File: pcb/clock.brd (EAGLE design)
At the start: 0 parts

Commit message: Started PCB
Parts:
- added C1: 0.1uF, rcl:C025-025X050
- added C2, C3: 10uF, rcl:C025-025X050
- added C4: 1000uF, rcl:E3,5-8
- added CN1: (no value), adafruit:DCJACK_2MM_PTH
- added JP1: FTDI, pinhead:1X06/90
- added JP2: (no value), pinhead:1X02
- added JP3: 74AHCT125, ic-package:DIL14
- added R1, R3, R4, R5: 470, rcl:0207/10
- added R2: 10K, rcl:0207/10
- added U1: ESP-01, diy-modules:WIRELESS-WIFI-ESP-01
- added U2: LD1117V33, my-custom:TO-220
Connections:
- new net +5V: C1.1, C4.+, CN1.PWR, JP1.3, JP3.14, U2.P$3
- new net DTR: JP1.6
- new net GND: C1.2, C2.2, C3.2, C4.-, CN1.GND, JP1.1, JP1.2, JP2.2, JP3.1, JP3.4, JP3.7, R5.1, U1.A1, U2.P$1
- new net GNDBREAK: CN1.GNDBREAK
- new net GPIO2: JP3.2, U1.B1
- new net N$1: JP2.1, R1.2
- new net N$2: R2.1, U1.B2, U1.C2
- new net N$3: R4.1, R5.2
- new net NP_DATA: JP3.3, R1.1
- new net RXD_3V3: R3.1, R4.2, U1.D1
- new net RXD_5V: JP1.5, R3.2
- new net TXD_3V3: JP3.5, U1.A2
- new net TXD_5V: JP1.4, JP3.6
- new net VCC: C2.1, C3.1, R2.2, U1.D2, U2.P$2, U2.P$4
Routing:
- net VCC: track 0.00 -> 62.3 mm
- net GPIO2: track 0.00 -> 41.7 mm
- net TXD_5V: track 0.00 -> 30.3 mm
- net TXD_3V3: track 0.00 -> 26.9 mm
- net NP_DATA: track 0.00 -> 17.9 mm
- net RXD_3V3: track 0.00 -> 17.7 mm
- net N$2: track 0.00 -> 17.7 mm
- net RXD_5V: track 0.00 -> 8.89 mm
- net N$3: track 0.00 -> 4.45 mm
- net N$1: track 0.00 -> 3.81 mm
- added copper zone on layer 1, net +5V
- added copper zone on layer 16, net GND
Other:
- board outline added: 76.2 x 71.1 mm
- board text added: "5V"
- board text added: "BLK"
- board text added: "GND"
- board text added: "GRN"

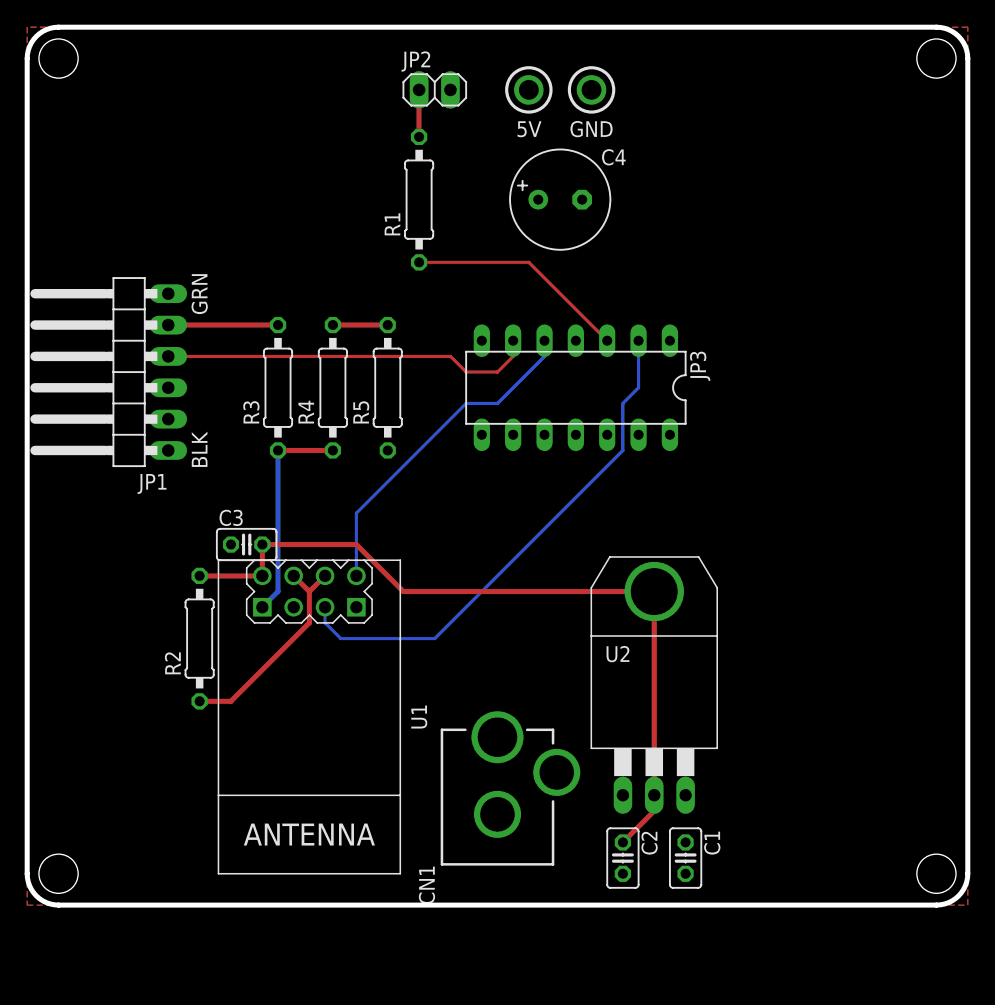
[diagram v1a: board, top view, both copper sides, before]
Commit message: Added button
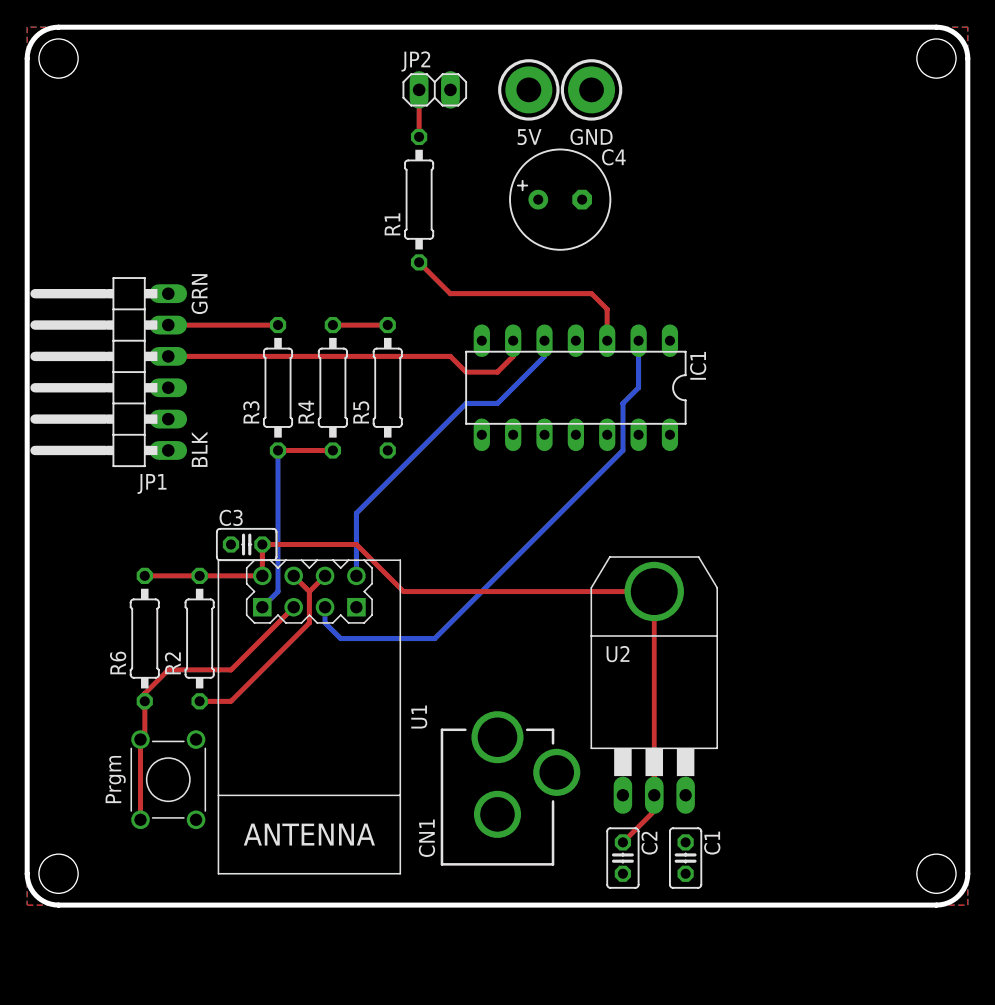
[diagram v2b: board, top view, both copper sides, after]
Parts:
- added R6: 10K, rcl:0207/10
- added S1: MJTP1230, my-custom:TACTILE-BUTTON-MJTP1230
- renumbered JP3 to IC1
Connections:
- new net GPIO0: R6.1, S1.P$1, S1.P$3, U1.C1
- net GND: now also S1.P$2, S1.P$4
- net VCC: now also R6.2
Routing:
- net GPIO0: track 0.00 -> 25.3 mm
- net VCC: track 62.3 -> 66.8 mm
- net NP_DATA: track 17.9 -> 19.4 mm
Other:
- board text added: "Prgm"

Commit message: Linearized the board layout
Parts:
- moved C4 44.5 mm to (41.9, 12.7)
- moved JP2 44.5 mm to (33.0, 21.6)
- moved JP1 42.0 mm to (10.2, 1.27), turned to 180 degrees
- moved R1 36.4 mm to (24.1, 21.6), turned to 180 degrees
- moved R6 36.1 mm to (41.9, 5.71), turned to 0 degrees
- moved IC1 33.8 mm to (25.4, 14.0)
- moved R2 33.8 mm to (41.9, 2.54), turned to 0 degrees
- moved C3 30.3 mm to (34.3, 3.81), turned to 90 degrees
- moved R5 28.8 mm to (7.62, 22.9), turned to 180 degrees
- moved R3 28.4 mm to (7.62, 16.5), turned to 180 degrees
- moved R4 28.1 mm to (7.62, 19.7), turned to 0 degrees
- moved CN1 25.4 mm to (63.5, 0.00)
- moved C2 20.1 mm to (59.7, 20.3), turned to 0 degrees
- moved C1 20.1 mm to (59.7, 22.9), turned to 180 degrees
- moved U2 5.68 mm to (53.3, 17.8), turned to 180 degrees
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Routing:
- net GPIO2: track 41.7 -> 16.1 mm
- net NP_DATA: track 19.4 -> 4.34 mm
- net TXD_5V: track 30.3 -> 18.9 mm
- net RXD_3V3: track 17.7 -> 28.1 mm
- net RXD_5V: track 8.89 -> 19.1 mm
- net N$1: track 3.81 -> 13.8 mm
- net VCC: track 66.8 -> 57.7 mm
- net TXD_3V3: track 26.9 -> 18.6 mm
- net GPIO0: track 25.3 -> 32.9 mm
- net N$2: track 17.7 -> 13.8 mm
- net N$3: track 4.45 -> 3.18 mm
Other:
- board size 76.2 x 71.1 mm -> 76.2 x 25.4 mm

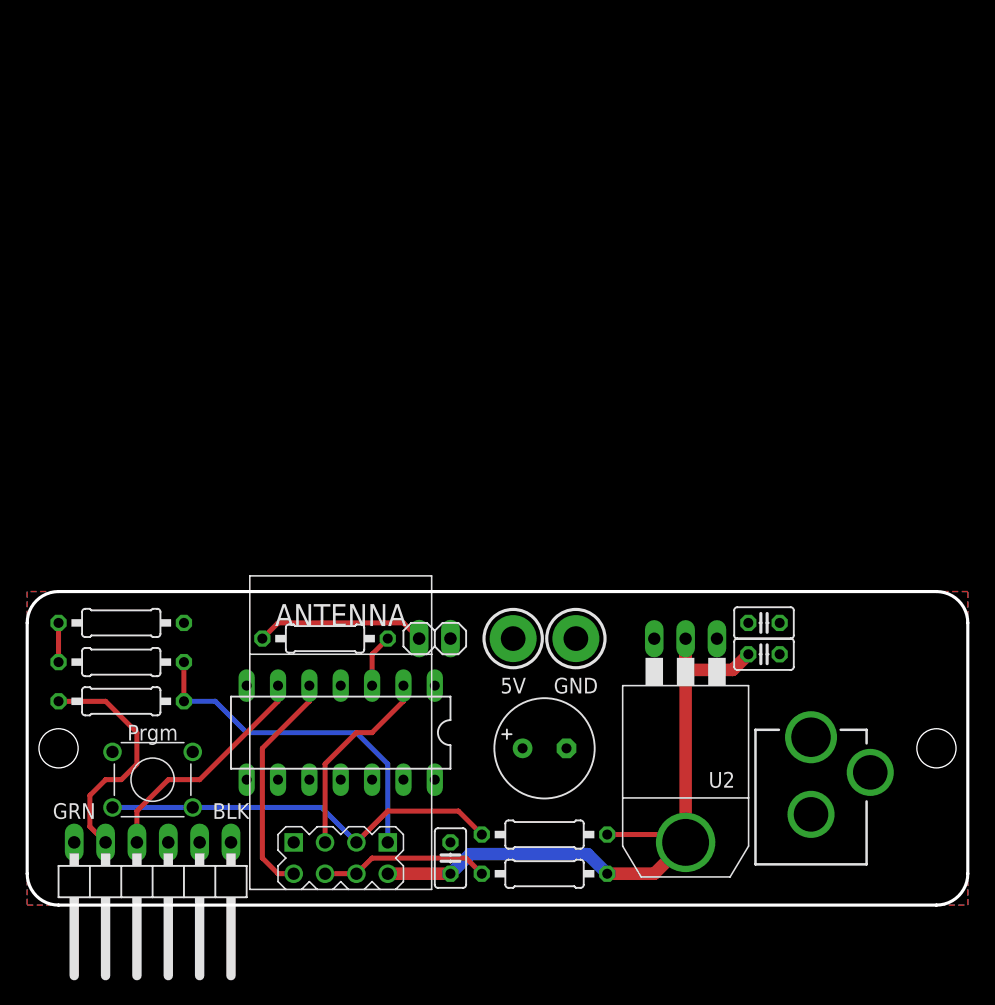
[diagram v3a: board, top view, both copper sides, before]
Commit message: Improved layout to make room for light sensor
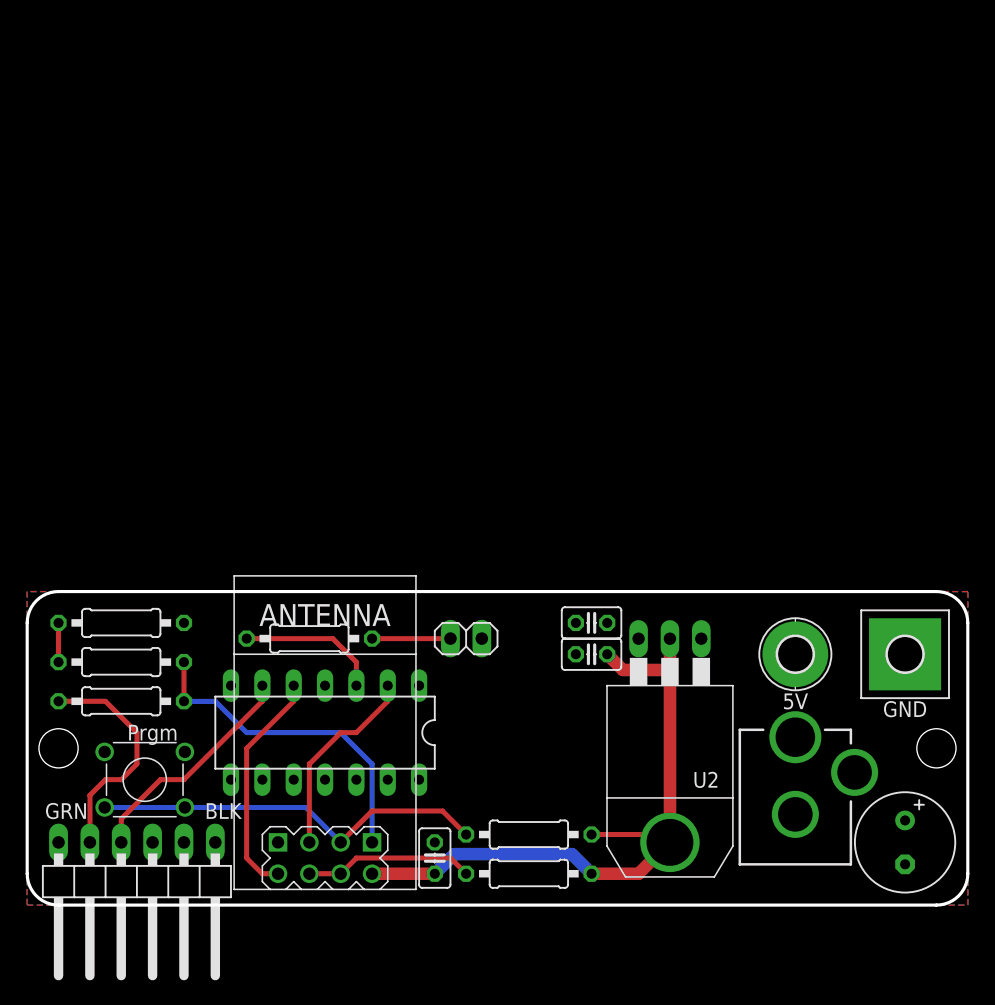
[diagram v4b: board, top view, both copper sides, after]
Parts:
- added H1: MOUNT-PAD-ROUND2.8, holes:2,8-PAD
- added H2: MOUNT-PAD-SQUARE2.8, holes:2,8-PAD-SQUARE
- moved C4 30.2 mm to (71.1, 5.08), turned to 270 degrees
- moved C1 14.0 mm to (45.7, 22.9), turned to 0 degrees
- moved C2 14.0 mm to (45.7, 20.3), turned to 180 degrees
- moved JP2 2.54 mm to (35.6, 21.6)
- moved CN1 1.27 mm to (62.2, 0.00)
- moved U2 1.27 mm to (52.1, 17.8)
- moved IC1 1.27 mm to (24.1, 14.0)
- moved JP1 1.27 mm to (8.89, 1.27)
- moved R1 1.27 mm to (22.9, 21.6), turned to 0 degrees
- moved U1 1.27 mm to (24.1, 14.0)
- moved C3 1.27 mm to (33.0, 3.81)
- moved R2 1.27 mm to (40.6, 2.54)
- moved R6 1.27 mm to (40.6, 5.71)
- moved S1 0.63 mm to (9.53, 10.2)
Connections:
- net +5V: now also H1.B2,8
- net GND: now also H2.B2,8
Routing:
- net N$1: track 13.8 -> 6.35 mm
- net NP_DATA: track 4.34 -> 11.6 mm
- net VCC: track 57.7 -> 55.2 mm
- net RXD_3V3: track 28.1 -> 26.9 mm
- net GPIO0: track 32.9 -> 32.3 mm
- net RXD_5V: track 19.1 -> 18.6 mm

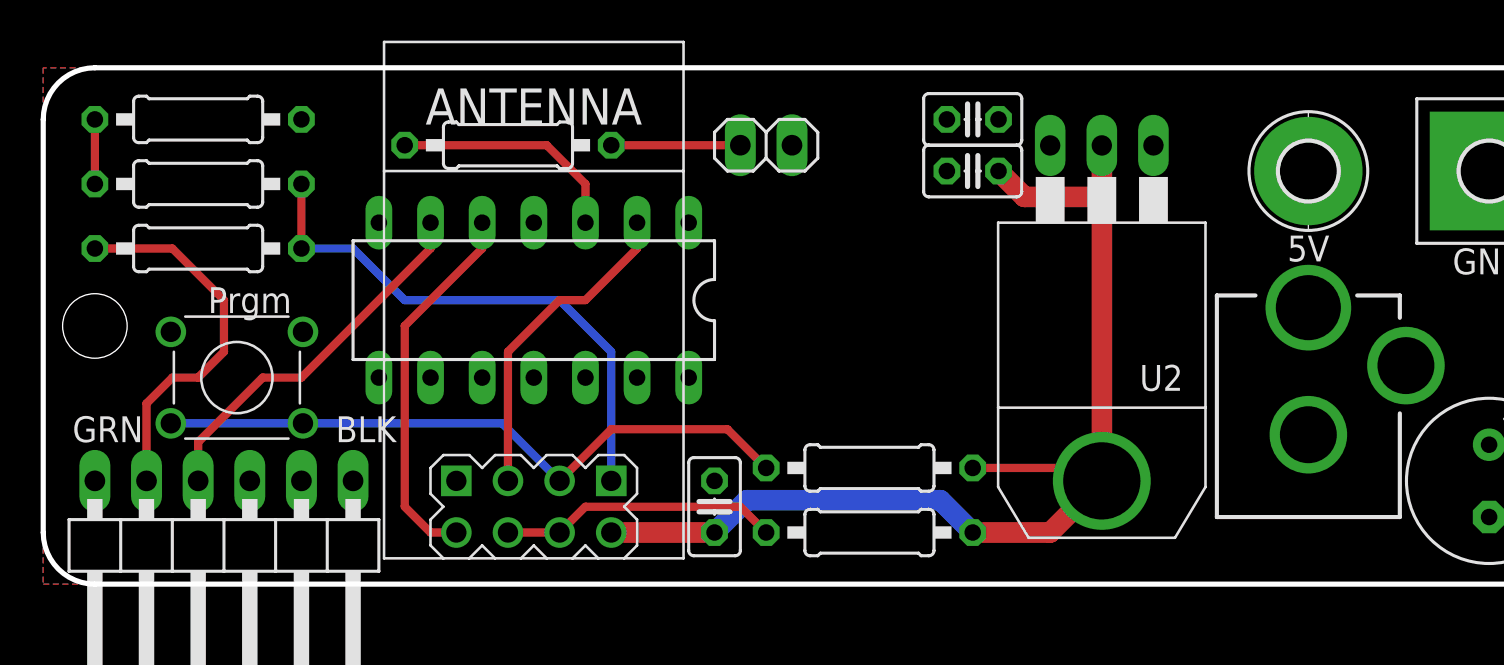
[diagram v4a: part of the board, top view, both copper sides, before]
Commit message: Added RP diode, tweaked layout
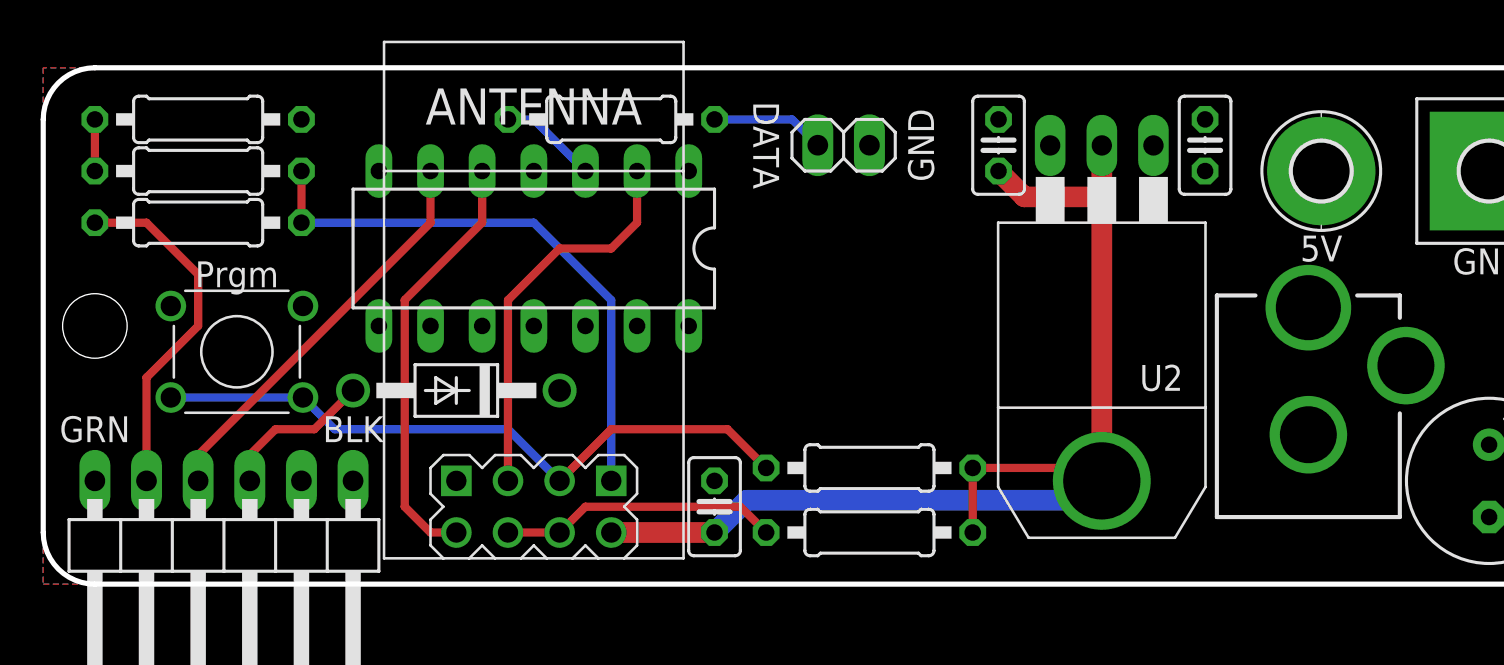
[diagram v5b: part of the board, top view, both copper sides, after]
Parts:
- added D1: 1N4004, diode:DO41-10
- moved C1 11.5 mm to (57.1, 21.6), turned to 90 degrees
- moved R1 5.24 mm to (27.9, 22.9)
- moved JP2 3.81 mm to (39.4, 21.6)
- moved IC1 2.54 mm to (24.1, 16.5)
- moved C2 1.80 mm to (47.0, 21.6), turned to 90 degrees
- moved R3 1.27 mm to (7.62, 17.8)
- moved S1 1.27 mm to (9.53, 11.4)
- moved H1 0.64 mm to (62.9, 20.3)
- moved R4 0.64 mm to (7.62, 20.3)
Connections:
- new net +5V_FTDI: D1.A, JP1.3
- net +5V: now also D1.C; no longer JP1.3
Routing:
- net +5V_FTDI: track 0.00 -> 7.67 mm
- net NP_DATA: track 11.6 -> 4.86 mm
- net GPIO2: track 16.1 -> 19.4 mm
- net TXD_3V3: track 18.6 -> 21.2 mm
- net VCC: track 55.2 -> 57.1 mm
- net TXD_5V: track 18.6 -> 20.0 mm
- net RXD_3V3: track 26.9 -> 28.2 mm
- net RXD_5V: track 18.6 -> 17.3 mm
- net N$1: track 6.35 -> 5.61 mm
- net N$3: track 3.18 -> 2.54 mm
- net GPIO0: track 32.3 -> 32.8 mm
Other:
- board text added: "DATA"

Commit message: Replaced 1N4004 with 1N5817
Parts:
- D1: value 1N4004 -> 1N5817-B; device diode:DO41-10 -> diode:DO41-7.6
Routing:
- net +5V_FTDI: track 7.67 -> 8.94 mm
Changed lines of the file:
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@@
 <element name="H1" library="holes" package="2,8-PAD" value="MOUNT-PAD-ROUND2.8" x="62.865" y="20.32"/>
 <element name="H2" library="holes" package="2,8-PAD-SQUARE" value="MOUNT-PAD-SQUARE2.8" x="71.12" y="20.32"/>
-<element name="D1" library="diode" package="DO41-10" value="1N4004" x="20.32" y="9.525" smashed="yes" rot="R180"/>
+<element name="D1" library="diode" package="DO41-7.6" value="1N5817-B" x="20.32" y="9.525" rot="R180"/>
 </elements>
 <signals>
@@
 <signal name="+5V_FTDI">
 <contactref element="JP1" pad="3"/>
-<contactref element="D1" pad="A"/>
 <wire x1="10.16" y1="5.08" x2="10.16" y2="6.35" width="0.4064" layer="1"/>
 <wire x1="10.16" y1="6.35" x2="11.43" y2="7.62" width="0.4064" layer="1"/>
-<wire x1="11.43" y1="7.62" x2="13.335" y2="7.62" width="0.4064" layer="1"/>
-<wire x1="13.335" y1="7.62" x2="15.24" y2="9.525" width="0.4064" layer="1"/>
+<wire x1="11.43" y1="7.62" x2="14.605" y2="7.62" width="0.4064" layer="1"/>
+<contactref element="D1" pad="A"/>
+<wire x1="14.605" y1="7.62" x2="16.51" y2="9.525" width="0.4064" layer="1"/>
 </signal>
 </signals>
